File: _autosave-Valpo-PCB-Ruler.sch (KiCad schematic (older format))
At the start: 2 parts, among them U1 ATtiny85-20PU

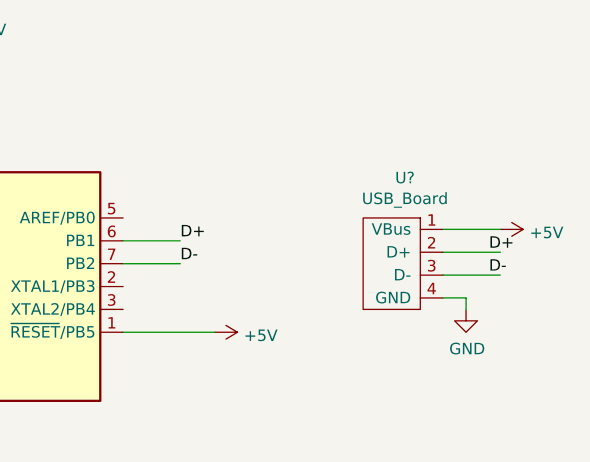
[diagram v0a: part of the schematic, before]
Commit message: Update basic design
Reduced size of ruler from 8in to 6in. Adjusted positioning of front masks and screens to match new size. Removed most of the references on the back to make room for the new circuitry to be included. Found initial components for USB circuitry (using ATtiny85).
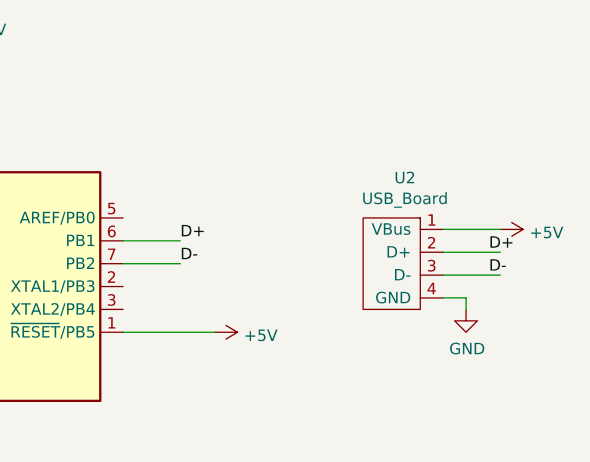
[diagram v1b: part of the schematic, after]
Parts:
- gave numbers to parts that had none: 1
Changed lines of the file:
@@
 	5300 2050 5550 2050
 $Comp
-L Valpo-PCB-Ruler:USB_Board U?
+L Valpo-PCB-Ruler:USB_Board U2
 U 1 1 6114E671
 P 6500 1900
-F 0 "U?" H 6533 2025 50  0000 C CNN
+F 0 "U2" H 6533 2025 50  0000 C CNN
 F 1 "USB_Board" H 6533 1934 50  0000 C CNN
 F 2 "Valpo-PCB-Ruler-FP:USB_Board" H 6500 1900 50  0001 C CNN
@@
 $EndComp
 $Comp
-L power:GND #PWR?
+L power:GND #PWR0103
 U 1 1 6114F3C4
 P 6800 2350
-F 0 "#PWR?" H 6800 2100 50  0001 C CNN
+F 0 "#PWR0103" H 6800 2100 50  0001 C CNN
 F 1 "GND" H 6805 2177 50  0000 C CNN
 F 2 "" H 6800 2350 50  0001 C CNN
@@
 $EndComp
 $Comp
-L power:+5V #PWR?
+L power:+5V #PWR0104
 U 1 1 61150D1A
 P 6950 2000
-F 0 "#PWR?" H 6950 1850 50  0001 C CNN
+F 0 "#PWR0104" H 6950 1850 50  0001 C CNN
 F 1 "+5V" V 6965 2128 50  0000 L CNN
 F 2 "" H 6950 2000 50  0001 C CNN
